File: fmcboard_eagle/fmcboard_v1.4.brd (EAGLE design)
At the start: 147 x 74 mm, 146 parts, among them IC1 OPA699ID, IC10 LTC6229IMS8E#TRPBF, IC11 7805TV, IC12 SN74AUC2G66DCTR, IC13 SN74AUC2G66DCTR, IC14 SN74AUC2G66DCTR, IC15 SN74AUC2G66DCTR, IC16 DAC7578SPWR, IC2 DAC7578SPWR, IC3 LTC6229IMS8E#TRPBF, IC4 LTC6229IMS8E#TRPBF, IC5 LM358, IC6 OPA699ID, IC7 OPA699ID, IC8 LTC6229IMS8E#TRPBF, IC9 LTC6229IMS8E#TRPBF, J1 8pin, J10 8pin, J12 4p-2.54, J2 ASP-134604-01, J3 4p-2.54, J4 4p-2.54, J5 8pin, J6 4p-2.54, J7 4p-2.54, J8 4p-2.54, J9 8pin, U1 TXS0108EPWR, U2 STMICROELECTRONICS_L7905ACVST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

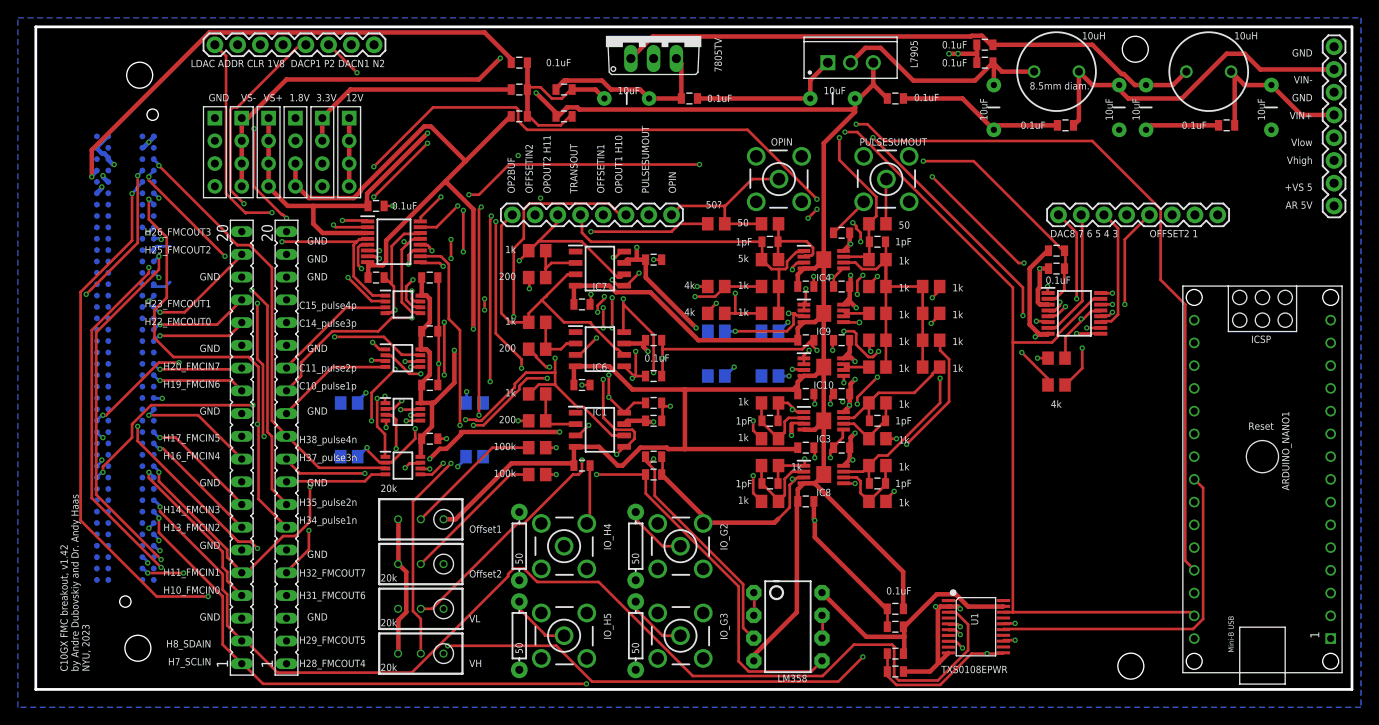
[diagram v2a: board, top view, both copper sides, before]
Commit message: 1.43 add caps on dac outs
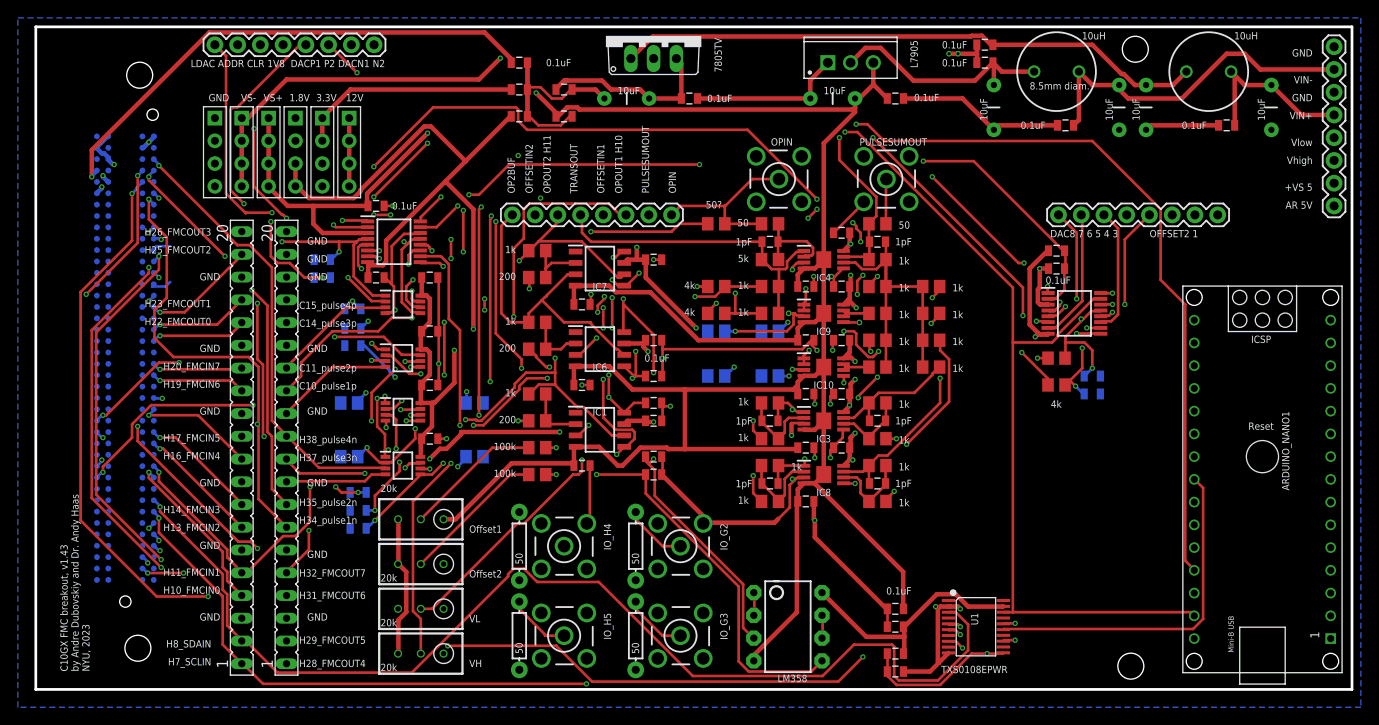
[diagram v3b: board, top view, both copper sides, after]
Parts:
- added C56, C57, C58, C59, C60, C61, C62, C63, C64, C65: 0.1uF, SparkFun-Passives:0805
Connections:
- net DACN1: now also C57.2
- net DACN2: now also C61.1
- net DACN3: now also C59.2
- net DACN4: now also C60.1
- net DACOFFSET1: now also C64.2
- net DACOFFSET2: now also C65.1
- net DACP1: now also C58.2
- net DACP2: now also C63.1
- net DACP3: now also C56.2
- net DACP4: now also C62.1
- net GND: now also C56.1, C57.1, C58.1, C59.1, C60.2, C61.2, C62.2, C63.2, C64.1, C65.2
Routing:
- net DACN1: track 42.9 -> 72.1 mm, vias 2 -> 4
- net DACP2: track 37.0 -> 52.3 mm, vias 2 -> 5
- net DACN2: track 53.5 -> 66.3 mm, vias 4 -> 6
- net DACN3: track 24.1 -> 33.8 mm, vias 2 -> 5
- net DACP4: track 17.1 -> 26.5 mm, vias 2 -> 3
- net DACN4: track 30.2 -> 38.8 mm, vias 2 -> 3
- net DACOFFSET2: track 28.4 -> 35.0 mm, vias 1 -> 2
- net DACOFFSET1: track 35.4 -> 38.3 mm, vias 2 -> 3
- net DACP1: track 46.7 -> 49.1 mm, vias 2 -> 3
- net DACP3: track 14.2 -> 15.9 mm, vias 2 -> 3
- net PULSEOUTN1: track 27.4 -> 26.6 mm, vias 5 -> 4
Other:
- board text added: "C10GX FMC breakout, v1.43 by Andre Dubovskiy and Dr. Andy Haas NYU, 2023"
- board text removed: "C10GX FMC breakout, v1.42 by Andre Dubovskiy and Dr. Andy Haas NYU, 2023"

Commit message: 1.43 switch SDA and SCL for DACs to A4/5, add 4.7k pullups on SDA/SCL lines
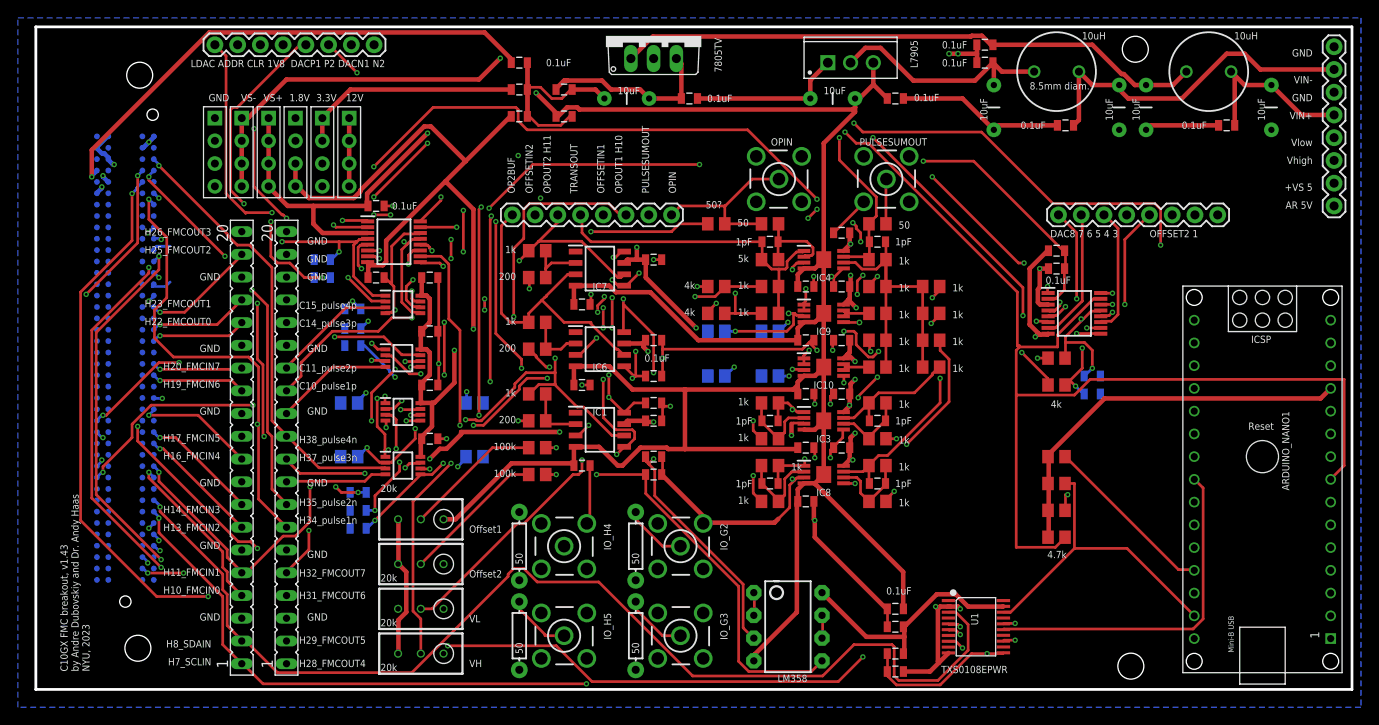
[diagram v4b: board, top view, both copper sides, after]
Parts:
- added R48, R49, R50, R51: 4.7k, rcl:R0805
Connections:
- new net AR_SCLIN2: ARDUINO_NANO1.9, IC16.16, IC2.16, R49.2
- new net AR_SDAIN2: ARDUINO_NANO1.8, IC16.15, IC2.15, R48.2
- net AR_5V: now also R48.1, R49.1, R50.1, R51.1
- net AR_SCLIN: now also R51.2; no longer IC16.16, IC2.16
- net AR_SDAIN: now also R50.2; no longer IC16.15, IC2.15
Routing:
- net AR_SDAIN2: track 0.00 -> 174.6 mm, vias 0 -> 4
- net AR_SCLIN2: track 0.00 -> 174.3 mm, vias 0 -> 5
- net AR_SCLIN: track 211.4 -> 44.4 mm, vias 4 -> 1
- net AR_SDAIN: track 147.5 -> 35.7 mm, vias 4 -> 0
- net AR_5V: track 21.4 -> 65.5 mm

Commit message: v1.43 100 -> 47 Ohm for pulses
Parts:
- R37, R39, R41, R43, R44, R45, R46, R47: value 100 -> 47
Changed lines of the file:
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@@
 <drawing>
 <settings>
-<setting alwaysvectorfont="no"/>
+<setting alwaysvectorfont="yes"/>
 <setting verticaltext="up"/>
 </settings>
@@
 <layers>
 <layer number="1" name="top" color="4" fill="1" visible="yes" active="yes"/>
-<layer number="2" name="topgnd" color="16" fill="1" visible="no" active="yes"/>
+<layer number="2" name="topgnd" color="16" fill="1" visible="yes" active="yes"/>
 <layer number="3" name="Route3" color="4" fill="3" visible="no" active="no"/>
 <layer number="4" name="Route4" color="1" fill="4" visible="no" active="no"/>
@@
 <layer number="14" name="Route14" color="1" fill="6" visible="no" active="no"/>
 <layer number="15" name="route" color="19" fill="1" visible="yes" active="yes"/>
-<layer number="16" name="gnd" color="1" fill="1" visible="no" active="yes"/>
+<layer number="16" name="gnd" color="1" fill="1" visible="yes" active="yes"/>
 <layer number="17" name="Pads" color="2" fill="1" visible="yes" active="yes"/>
 <layer number="18" name="Vias" color="2" fill="1" visible="yes" active="yes"/>
@@
 <attribute name="PROD_ID" value="CONN-08438" x="132" y="53" size="1.778" layer="27" rot="R180" display="off"/>
 </element>
-<element name="R37" library="rcl" library_urn="urn:adsk.eagle:library:334" package="R0805" package3d_urn="urn:adsk.eagle:package:23553/2" value="100" x="82" y="40" smashed="yes" rot="MR180">
+<element name="R37" library="rcl" library_urn="urn:adsk.eagle:library:334" package="R0805" package3d_urn="urn:adsk.eagle:package:23553/2" value="47" x="82" y="40" smashed="yes" rot="MR180">
 <attribute name="POPULARITY" value="85" x="82" y="40" size="1.778" layer="28" rot="MR180" display="off"/>
 <attribute name="SPICEPREFIX" value="R" x="82" y="40" size="1.778" layer="28" rot="MR180" display="off"/>
 <attribute name="VALUE" x="82.635" y="41.46" size="0.8128" layer="22" rot="MR0"/>
 </element>
-<element name="R39" library="rcl" library_urn="urn:adsk.eagle:library:334" package="R0805" package3d_urn="urn:adsk.eagle:package:23553/2" value="100" x="76" y="40" smashed="yes" rot="MR0">
+<element name="R39" library="rcl" library_urn="urn:adsk.eagle:library:334" package="R0805" package3d_urn="urn:adsk.eagle:package:23553/2" value="47" x="76" y="40" smashed="yes" rot="MR0">
 <attribute name="POPULARITY" value="85" x="76" y="40" size="1.778" layer="28" rot="MR0" display="off"/>
 <attribute name="SPICEPREFIX" value="R" x="76" y="40" size="1.778" layer="28" rot="MR0" display="off"/>
 <attribute name="VALUE" x="76.635" y="41.46" size="0.8128" layer="22" rot="MR0"/>
 </element>
-<element name="R41" library="rcl" library_urn="urn:adsk.eagle:library:334" package="R0805" package3d_urn="urn:adsk.eagle:package:23553/2" value="100" x="82" y="35" smashed="yes" rot="MR180">
+<element name="R41" library="rcl" library_urn="urn:adsk.eagle:library:334" package="R0805" package3d_urn="urn:adsk.eagle:package:23553/2" value="47" x="82" y="35" smashed="yes" rot="MR180">
 <attribute name="POPULARITY" value="85" x="82" y="35" size="1.778" layer="28" rot="MR180" display="off"/>
 <attribute name="SPICEPREFIX" value="R" x="82" y="35" size="1.778" layer="28" rot="MR180" display="off"/>
 <attribute name="VALUE" x="82.635" y="36.46" size="0.8128" layer="22" rot="MR0"/>
 </element>
-<element name="R43" library="rcl" library_urn="urn:adsk.eagle:library:334" package="R0805" package3d_urn="urn:adsk.eagle:package:23553/2" value="100" x="76" y="35" smashed="yes" rot="MR0">
+<element name="R43" library="rcl" library_urn="urn:adsk.eagle:library:334" package="R0805" package3d_urn="urn:adsk.eagle:package:23553/2" value="47" x="76" y="35" smashed="yes" rot="MR0">
 <attribute name="POPULARITY" value="85" x="76" y="35" size="1.778" layer="28" rot="MR0" display="off"/>
 <attribute name="SPICEPREFIX" value="R" x="76" y="35" size="1.778" layer="28" rot="MR0" display="off"/>
 <attribute name="VALUE" x="76.635" y="36.46" size="0.8128" layer="22" rot="MR0"/>
 </element>
-<element name="R44" library="rcl" library_urn="urn:adsk.eagle:library:334" package="R0805" package3d_urn="urn:adsk.eagle:package:23553/2" value="100" x="35" y="32" smashed="yes" rot="MR0">
+<element name="R44" library="rcl" library_urn="urn:adsk.eagle:library:334" package="R0805" package3d_urn="urn:adsk.eagle:package:23553/2" value="47" x="35" y="32" smashed="yes" rot="MR0">
 <attribute name="POPULARITY" value="85" x="35" y="32" size="1.778" layer="28" rot="MR0" display="off"/>
 <attribute name="SPICEPREFIX" value="R" x="35" y="32" size="1.778" layer="28" rot="MR0" display="off"/>
 <attribute name="VALUE" x="35.635" y="33.46" size="0.8128" layer="22" rot="MR0"/>
 </element>
-<element name="R45" library="rcl" library_urn="urn:adsk.eagle:library:334" package="R0805" package3d_urn="urn:adsk.eagle:package:23553/2" value="100" x="35" y="26" smashed="yes" rot="MR0">
+<element name="R45" library="rcl" library_urn="urn:adsk.eagle:library:334" package="R0805" package3d_urn="urn:adsk.eagle:package:23553/2" value="47" x="35" y="26" smashed="yes" rot="MR0">
 <attribute name="POPULARITY" value="85" x="35" y="26" size="1.778" layer="28" rot="MR0" display="off"/>
 <attribute name="SPICEPREFIX" value="R" x="35" y="26" size="1.778" layer="28" rot="MR0" display="off"/>
 <attribute name="VALUE" x="35.635" y="27.46" size="0.8128" layer="22" rot="MR0"/>
 </element>
-<element name="R46" library="rcl" library_urn="urn:adsk.eagle:library:334" package="R0805" package3d_urn="urn:adsk.eagle:package:23553/2" value="100" x="49" y="26" smashed="yes" rot="MR0">
+<element name="R46" library="rcl" library_urn="urn:adsk.eagle:library:334" package="R0805" package3d_urn="urn:adsk.eagle:package:23553/2" value="47" x="49" y="26" smashed="yes" rot="MR0">
 <attribute name="POPULARITY" value="85" x="49" y="26" size="1.778" layer="28" rot="MR0" display="off"/>
 <attribute name="SPICEPREFIX" value="R" x="49" y="26" size="1.778" layer="28" rot="MR0" display="off"/>
 <attribute name="VALUE" x="49.635" y="27.46" size="0.8128" layer="22" rot="MR0"/>
 </element>
-<element name="R47" library="rcl" library_urn="urn:adsk.eagle:library:334" package="R0805" package3d_urn="urn:adsk.eagle:package:23553/2" value="100" x="49" y="32" smashed="yes" rot="MR0">
+<element name="R47" library="rcl" library_urn="urn:adsk.eagle:library:334" package="R0805" package3d_urn="urn:adsk.eagle:package:23553/2" value="47" x="49" y="32" smashed="yes" rot="MR0">
 <attribute name="POPULARITY" value="85" x="49" y="32" size="1.778" layer="28" rot="MR0" display="off"/>
 <attribute name="SPICEPREFIX" value="R" x="49" y="32" size="1.778" layer="28" rot="MR0" display="off"/>

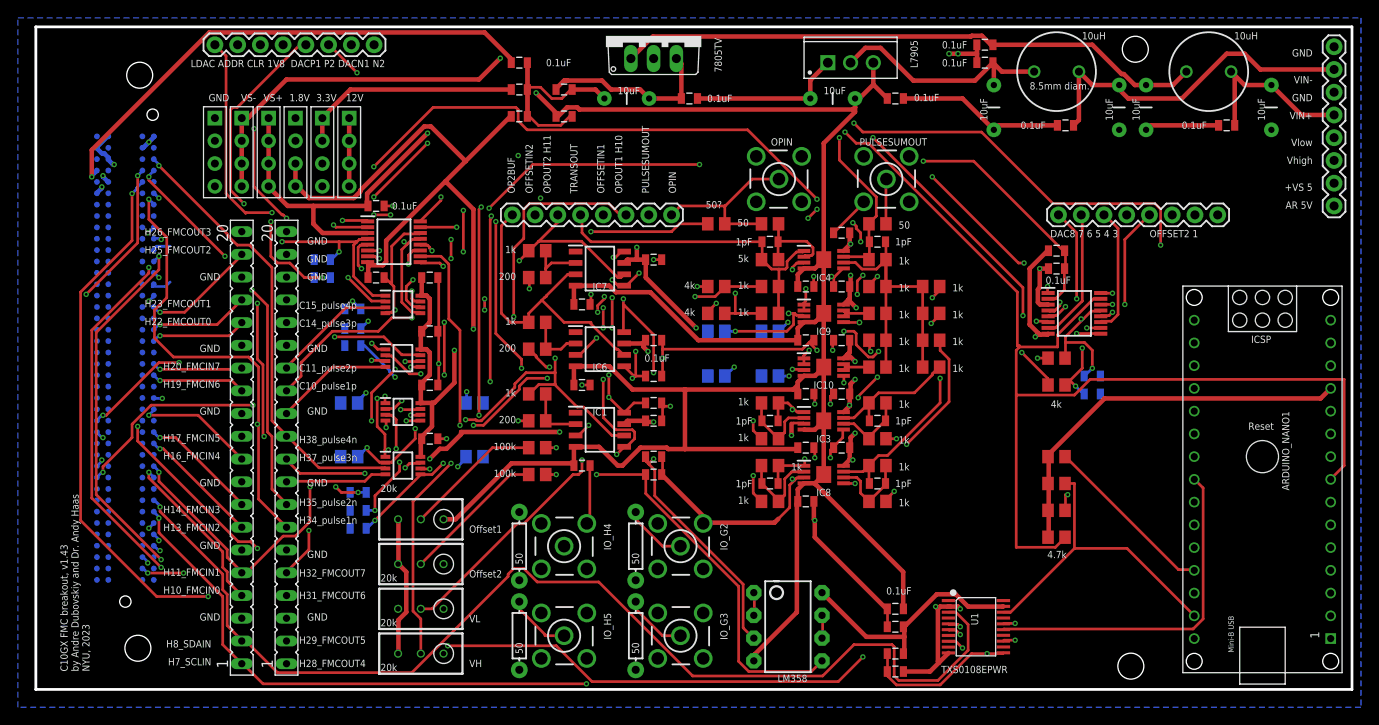
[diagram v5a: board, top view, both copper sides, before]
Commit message: Put all components on top
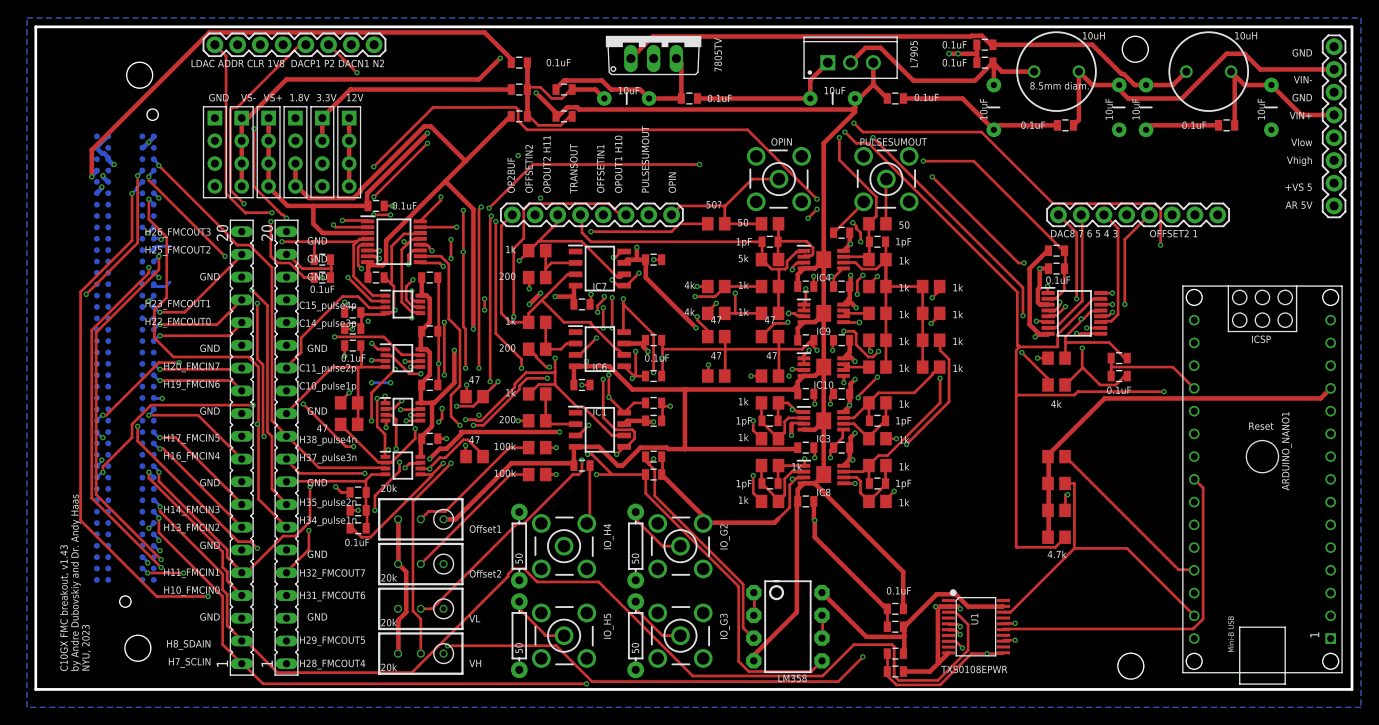
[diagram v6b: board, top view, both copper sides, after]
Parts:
- moved C64 3.61 mm to (121.0, 35.0), flipped to the top
- moved C65 3.61 mm to (121.0, 37.0), flipped to the top
- moved R45 3.60 mm to (35.0, 29.6), flipped to the top
- moved R47 0.70 mm to (49.0, 32.7), flipped to the top
- moved R37 0.60 mm to (82.0, 39.4), flipped to the top
- moved R39 0.60 mm to (76.0, 39.4), flipped to the top
- moved C63 0.40 mm to (35.4, 42.1), flipped to the top
- flipped C56 to the top
- flipped C57 to the top
- flipped C58 to the top
- flipped C59 to the top
- flipped C60 to the top
- flipped C61 to the top
- flipped C62 to the top
- flipped R41 to the top
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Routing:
- net GND: track 366.9 -> 418.1 mm, vias 33 -> 35
- net C10: track 71.3 -> 101.9 mm, vias 7 -> 12
- net OFFSETIN2: track 88.2 -> 104.1 mm, vias 4 -> 6
- net VS-: track 316.3 -> 304.2 mm, vias 2 -> 6
- net AR_SDAIN2: track 174.6 -> 164.9 mm, vias 4 -> 5
- net PULSEINN4: track 57.5 -> 64.0 mm, vias 3 -> 2
- net PULSEINP1: track 92.4 -> 86.3 mm
- net DACN4: track 38.8 -> 43.5 mm, vias 3 -> 2
- net DACOFFSET1: track 38.3 -> 42.3 mm, vias 3 -> 2
- net DACP4: track 26.5 -> 29.5 mm, vias 3 -> 5
- net PULSEINN3: track 54.9 -> 57.3 mm, vias 3 -> 2
- net PULSEINN2: track 63.5 -> 61.3 mm, vias 3 -> 4
- net PULSEINP2: track 63.4 -> 65.6 mm
- net C11: track 43.9 -> 45.9 mm
- net DACP3: track 15.9 -> 17.8 mm, vias 3 -> 4
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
